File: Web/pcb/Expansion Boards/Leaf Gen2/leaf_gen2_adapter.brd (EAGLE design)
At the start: 154.2 x 104.1 mm, 20 parts, among them CN101 GT8E-5P-DS, CN151 GT8E-12DP-DS, CN501 GT8E-16DP-DS, CN601 GT8E-8P-DS, IC1 SN74F00N, J1 LEAFMAIN

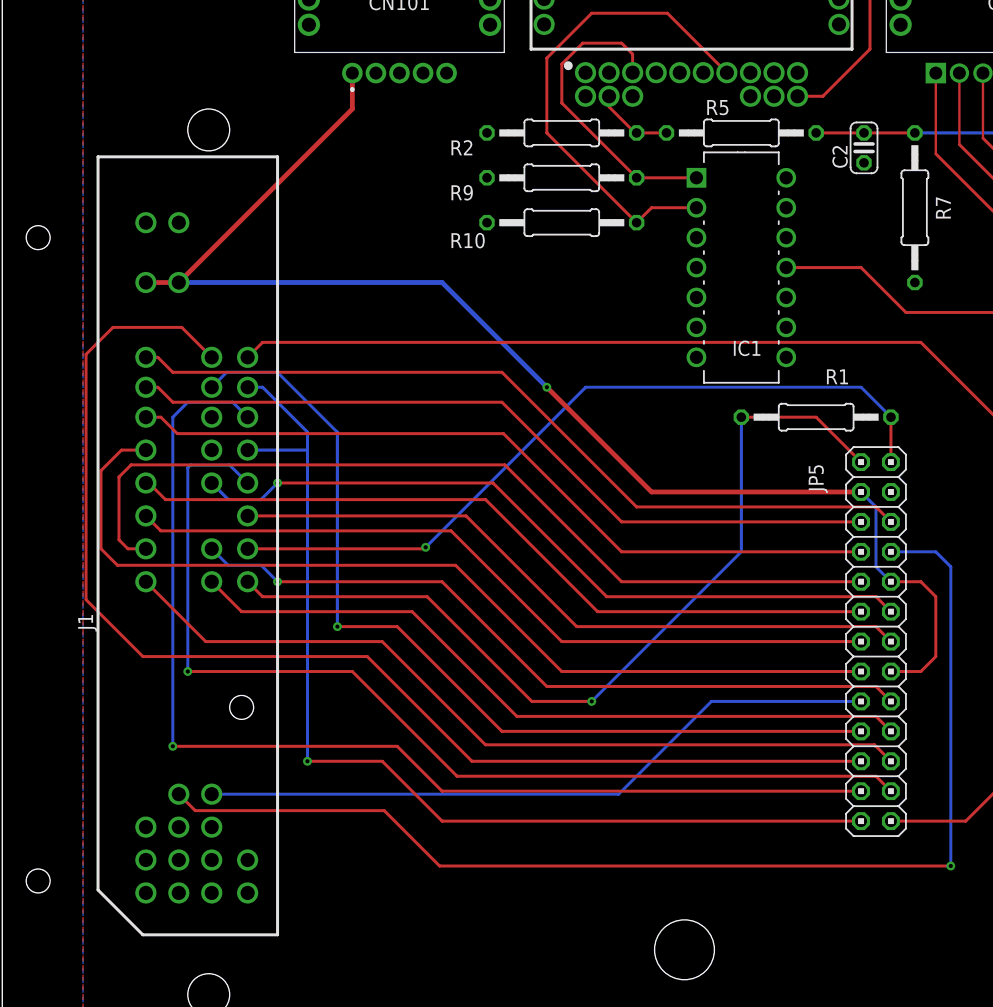
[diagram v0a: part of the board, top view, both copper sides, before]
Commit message: esp fix
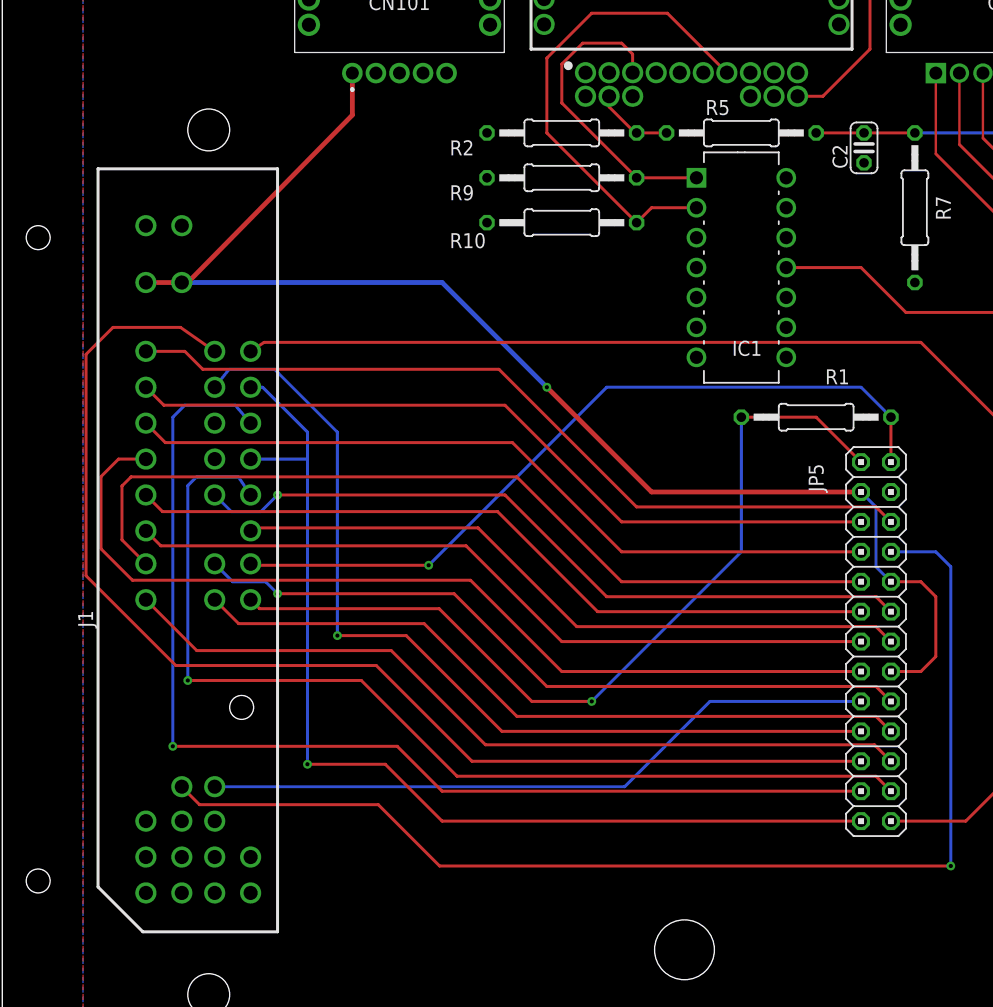
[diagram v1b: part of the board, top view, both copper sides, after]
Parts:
- moved J1 0.25 mm to (-115.6, -15.7)
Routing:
- net THROTTLE1: track 105.0 -> 103.6 mm
- net OUT_TEMP: track 75.5 -> 74.2 mm
- net CANH: track 74.5 -> 73.7 mm
- net SIG_START: track 62.9 -> 62.0 mm
- net SIG_BRAKE: track 63.0 -> 62.2 mm
- net SIG_REVERSE: track 63.4 -> 62.7 mm
- net SIG_CRUISE: track 69.6 -> 68.9 mm
- net OUT_DCSW: track 80.0 -> 79.4 mm
- net SIG_FORWARD: track 59.0 -> 58.5 mm
- net RES_S3: track 108.3 -> 107.8 mm
- net OUT_ERR: track 65.1 -> 64.6 mm
- net OUT_BRAKE: track 58.4 -> 57.9 mm
- net THROTTLE2: track 77.9 -> 78.4 mm
